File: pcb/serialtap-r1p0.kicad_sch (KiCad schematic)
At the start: 0 parts

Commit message: Capture the schematic, and correct the connector pin numbering
Two things that turned out to be one commit, because splitting them would
have left a snapshot where the schematic and the bench notes disagree about
which pin is which.

**The schematic is drawn.** `pcb/serialtap-r1p0.kicad_sch`, KiCad 10 native,
one A3 sheet in seven blocks, 43 components and 57 nets, transcribed from the
wiring contract in docs/schematic-capture.md. `kicad-cli sch erc
--severity-all` reports 0 violations, and every review invariant was checked
against the extracted netlist rather than the drawing — a drawing can look
right and still be wrong.

Decided at capture, with reasoning in docs/schematic-capture.md:

- `RILIM` = 66.5 kohm 1%, a 351-449 mA limit once part and resistor tolerance
  are counted: above the board's 250 mA worst case so a Wi-Fi burst cannot
  nuisance-trip it, below the rail's OEM-implied capability (ADR 0007)
- FAULT, PG and ST go to test pads, not GPIOs. Zero BOM cost, no firmware
  coupling; the cost is that no fault state reaches Home Assistant
- LM66200 VOUT_2 becomes a passive pin. Pins 2 and 7 are one internal node,
  and two power outputs on a net is an ERC conflict. The departure from the
  datasheet I/O column is recorded in lib/README.md
- Eleven generic symbols (R, C, LED, SW_Push, TestPoint, PWR_FLAG and the
  rails) copied in from KiCad 10, so the design still references nothing
  outside this repo. Passives carry no footprint: the package follows the MPN,
  and those are not pinned yet

kicad-happy review gate 1 ran. Of four non-informational findings, three
triage out and one is real and now accepted rather than fixed: USB VBUS has no
TVS, and reaches the LM66200's 6 V absolute maximum unclamped. The USB port is
a one-off setup interface and the operational path is J1, so the exposure is
closer to a debug header's.

**The service connector was being read from the wrong end.** Corrected order
is 5 V, TX, RX, spare, GND; old pin n is new pin 6 - n. Noth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
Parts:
- added C1, C7, C8, C9: 0.1u, symbol serialtap:C
- added C10, C5: 10u, symbol serialtap:C
- added C11, C2, C3: 1u, symbol serialtap:C
- added C4: 470u, symbol serialtap:C
- added C6: 22u, symbol serialtap:C
- added D1: LED, symbol serialtap:LED
- added J1: B05B-XASK-1-A, serialtap:JST_XA_B05B-XASK-1-A_1x05_P2.50mm_Vertical, symbol serialtap:B05B-XASK-1-A
- added J2: USB4085-GF-A, serialtap:USB_C_Receptacle_GCT_USB4085, symbol serialtap:USB4085-GF-A
- added L1: XGL4020-222MEC, serialtap:L_Coilcraft_XGL4020_4.0x4.0mm, symbol serialtap:XGL4020-222MEC
- added R1, R2: 330, symbol serialtap:R
- added R10, R9: 10k, symbol serialtap:R
- added R3, R4, R8: 5.1k, symbol serialtap:R
- added R5: 66.5k, symbol serialtap:R
- added R6, R7: 100k, symbol serialtap:R
- added SW1, SW2: SW_Push, symbol serialtap:SW_Push
- added TP1, TP10, TP2, TP3, TP4, TP5, TP6, TP7, TP8, TP9: TestPoint, symbol serialtap:TestPoint
- added U1: TPS2553DBV, serialtap:SOT-23-6, symbol serialtap:TPS2553DBV
- added U2: LM66200DRL, serialtap:TI_DRL0008A_SOT-5X3-8_2.1x1.6mm_P0.5mm, symbol serialtap:LM66200DRL
- added U3: TPS62162DSG, serialtap:Texas_DSG0008A_WSON-8-1EP_2x2mm_P0.5mm_EP0.9x1.6mm_ThermalVias, symbol serialtap:TPS62162DSG
- added U4: TXU0204RUT, serialtap:TI_RUT0012A_UQFN-12_2.0x1.7mm_P0.4mm, symbol serialtap:TXU0204RUT
- added U5: TPD4E05U06DQA, serialtap:USON-10_2.5x1.0mm_P0.5mm, symbol serialtap:TPD4E05U06DQA
- added U6: ESP32-C3-MINI-1, serialtap:ESP32-C3-MINI-1, symbol serialtap:ESP32-C3-MINI-1
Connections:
- new net: J2.A5 (CC1), R3.1
- new net: J2.B5 (CC2), R4.1
- new net: L1.1, U3.7 (SW)
- new net: R5.1, U1.5 (ILIM)
- new net: D1.2 (A), R8.2
- new net BOOT: R9.2, SW1.2, U6.23 (GPIO9)
- new net C3_EN: C11.1, R10.2, SW2.2, U6.8 (EN/CHIP_PU)
- new net C3_RX: TP7.1, U4.4 (A3Y), U6.19 (GPIO5/ADC2_CH0)
- new net C3_TX: TP6.1, U4.2 (A1), U6.18 (GPIO4/ADC1_CH4)
- new net EFUSE_OUT: C2.1, U1.6 (OUT), U2.3 (VIN1)
- new net FAULT_N: R6.2, TP8.1, U1.4 (~{FAULT})
- new net GND: C1.2, C10.2, C11.2, C2.2, C3.2, C4.2, C5.2, C6.2, C7.2, C8.2, C9.2, D1.1 (K), J1.5 (Pin_5), J2.A1 (GND), J2.A12 (GND), J2.B1 (GND), J2.B12 (GND), J2.SH (SHIELD), R3.2, R4.2, R5.2, SW1.1, SW2.1, TP3.1, U1.2 (GND), U2.1 (GND_1), U2.4 (~{ON}), U2.5 (GND_2), U3.1 (PGND), U3.4 (AGND), U3.5 (FB), U3.9 (PAD), U4.3 (A2), U4.6 (GND), U4.7 (B4), U5.3 (GND), U5.8 (GND), U6.1 (GND), U6.11 (GND), U6.14 (GND), U6.2 (GND), U6.36 (GND), U6.37 (GND), U6.38 (GND), U6.39 (GND), U6.40 (GND), U6.41 (GND), U6.42 (GND), U6.43 (GND), U6.44 (GND), U6.45 (GND), U6.46 (GND), U6.47 (GND), U6.48 (GND), U6.49 (GND), U6.50 (GND), U6.51 (GND), U6.52 (GND), U6.53 (GND)
- new net PG: R7.2, TP9.1, U3.8 (PG)
- new net PORT_5V: C1.1, J1.1 (Pin_1), U1.1 (IN), U1.3 (EN)
- new net PORT_RX: J1.3 (Pin_3), R2.1, U5.2 (D1-)
- new net PORT_TX: J1.2 (Pin_2), R1.1, U5.1 (D1+)
- new net RX_BUF: R2.2, TP5.1, U4.8 (B3)
- new net ST: TP10.1, U2.8 (ST)
- new net TX_BUF: R1.2, TP4.1, U4.10 (B1Y)
- new net USB_DM: J2.A7 (D-), J2.B7 (D-), U5.5 (D2-), U6.26 (GPIO18/USB_D-)
- new net USB_DP: J2.A6 (D+), J2.B6 (D+), U5.4 (D2+), U6.27 (GPIO19/USB_D+)
- new net USB_VBUS: C3.1, J2.A4 (VBUS), J2.A9 (VBUS), J2.B4 (VBUS), J2.B9 (VBUS), U2.6 (VIN2)
- new net V3V3: C10.1, C6.1, C7.1, C9.1, L1.2, R10.1, R7.1, R9.1, TP2.1, U3.6 (VOS), U4.1 (VCCA), U4.12 (OE), U6.3 (3V3)
- new net V5: C4.1, C5.1, C8.1, R6.1, R8.1, TP1.1, U2.2 (VOUT_1), U2.7 (VOUT_2), U3.2 (VIN), U3.3 (EN), U4.11 (VCCB)
- no-connect marks 0 -> 19
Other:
- note added: "A Service port - J1, ESD, UART series protection"
- note added: "B USB-C - programming, logging, bench power"
- note added: "Both sides of each translator channel, both rails, GND,"
- note added: "C Power path - eFuse, ideal-diode OR, 3.3 V buck"
- note added: "Channels 1 and 2 run A to B, 3 and 4 run B to A."
- note added: "D Level translation - fixed direction, 3.3 V <-> 5 V"
- note added: "Direction is fixed in silicon - ADR 0001."
- note added: "E ESP32-C3-MINI-1 - USB, UART, recovery"
- note added: "ESD channels tap each line on the connector side,"
- note added: "F Test access - SPDD 5.7"
- note added: "G ERC power sources"
- note added: "GPIO4 = UART1 TX, GPIO5 = UART1 RX, to the A side of U4."
- note added: "J1 pin 4: function unknown, deliberately unconnected"
- note added: "R5 sets the limit above the board's 250 mA worst case and"
- note added: "Shield to GND; no VBUS path to PORT_5V except through U2"
- note added: "Spare GPIOs carry explicit no-connects - ADR 0002."
- note added: "U1 EN is tied to IN: the appliance branch is always enabled."
- note added: "U3 FB goes to AGND and VOS senses at C6, per the datasheet;"
- note added: "V5 is driven by U2's output pin. The other three supplies enter"
- note added: "VOS is in the control loop - see docs/layout-rules.md."
- note added: "ahead of R1/R2 and of the USB pair"
- note added: "and the three diagnostic pins."
- note added: "below the rail's OEM-implied capability - ADR 0007."
- note added: "on passive connector pins, so each needs a flag for ERC."

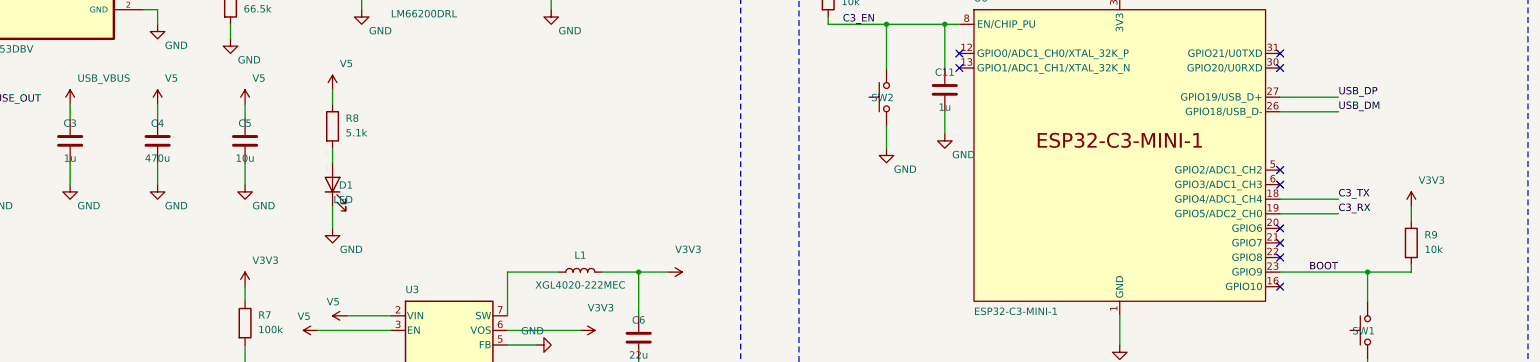
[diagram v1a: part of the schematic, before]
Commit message: Pin every passive, and let the switch datasheet move a resistor
Closes the last part-detail gate: all 22 BOM lines now carry an MPN, a
footprint and a datasheet. ~US$13.82/board.

Chosen as two families rather than line by line, because consistency is
worth more here than per-line optimisation:

- One KOA RK73H 1J series for every resistor value: 1%, 100 ppm/degC,
  -55..+155 C. The 66.5 kohm RILIM has to be 1% because the TPS2553
  datasheet says so, and running that grade everywhere costs cents and
  removes a class of mistake. Size code 1J = 0603 and tolerance code F =
  1% confirmed from the ordering table
- One Samsung CL series for every ceramic, X7R only and >=25 V. The
  TPS62162's LC stability table assumes variation stays inside +-20%
  *including DC bias*, which rules out X5R and 16 V parts on a 5 V rail.
  Samsung publish no per-part bias curve, so the retention estimate is
  labelled inference, not vendor data
- LTST-C191KGKT for the power LED: -55..+85 C, chosen over a 5x brighter
  emerald-green sibling for temperature grade, consistent with the
  H-grade module and the -Q1 ESD array. Dim is intended (SPDD 5.7)

**The switch datasheet changed a resistor.** C&K specify a 1 mA minimum
contact current; with a 10 kohm pull-up SW1 would have switched 0.33 mA,
a third of that, in the dry-circuit region where contact films do not
break down. R9 is therefore 2.2 kohm, putting 1.5 mA through SW1. R10
stays 10 kohm: SW2 discharges C11 through its contacts on every press,
which is a far larger wetting pulse, and shortening the EN time constant
would be the wrong move while the manual-reset anomaly is unexplained.

KMR211NGLFS's `NG` is the ordering key's no-ground-pin option, which is
what picks the four-pad land pattern over the five-pad one. C&K's
recommended layout - 0.9 x 1.0 mm pads at +-2.05, +-0.8 mm - matches
KiCad's footprint exactly. The datasheet had to be fetched by hand;
C&K and Littelfuse both refuse automated access.

Two capture defects, found by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
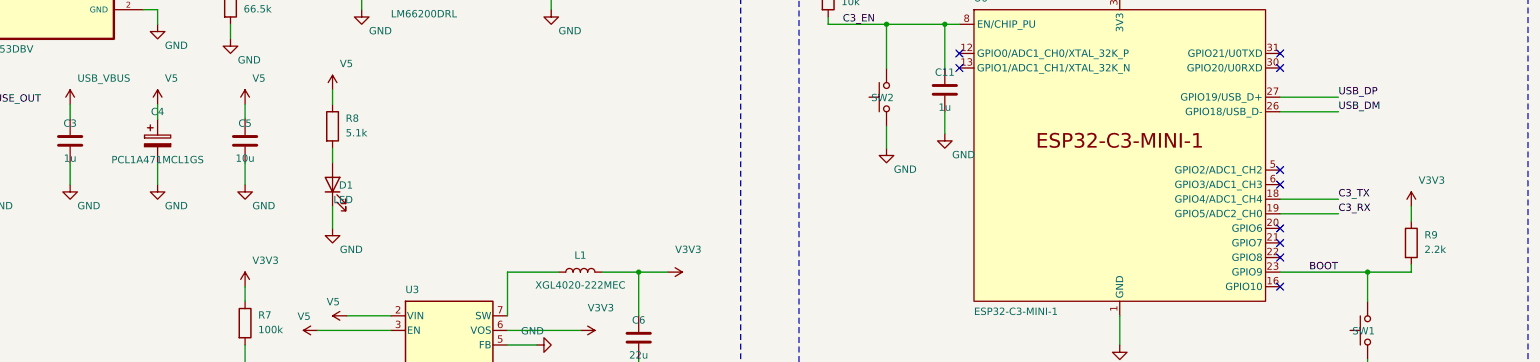
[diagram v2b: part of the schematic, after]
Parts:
- C1, C7, C8, C9: footprint (none) -> serialtap:C_0603_1608Metric; MPN (none) -> CL10B104KB8NNNC; Manufacturer (none) -> Samsung Electro-Mechanics
- C10, C5: footprint (none) -> serialtap:C_1206_3216Metric; MPN (none) -> CL31B106KAHNNNE; Manufacturer (none) -> Samsung Electro-Mechanics
- C11, C2, C3: footprint (none) -> serialtap:C_0603_1608Metric; MPN (none) -> CL10B105KA8NNNC; Manufacturer (none) -> Samsung Electro-Mechanics
- C4: value 470u -> PCL1A471MCL1GS; footprint (none) -> serialtap:CP_Elec_8x10; symbol serialtap:C -> serialtap:PCL1A471MCL1GS; MPN (none) -> PCL1A471MCL1GS; Manufacturer (none) -> Nichicon
- C6: footprint (none) -> serialtap:C_1210_3225Metric; MPN (none) -> CL32B226KAJNNNE; Manufacturer (none) -> Samsung Electro-Mechanics
- D1: footprint (none) -> serialtap:LED_0603_1608Metric; MPN (none) -> LTST-C191KGKT; Manufacturer (none) -> Lite-On
- R1, R2: footprint (none) -> serialtap:R_0603_1608Metric; MPN (none) -> RK73H1JTTD3300F; Manufacturer (none) -> KOA Speer
- R10: footprint (none) -> serialtap:R_0603_1608Metric; MPN (none) -> RK73H1JTTD1002F; Manufacturer (none) -> KOA Speer
- R3, R4, R8: footprint (none) -> serialtap:R_0603_1608Metric; MPN (none) -> RK73H1JTTD5101F; Manufacturer (none) -> KOA Speer
- R5: footprint (none) -> serialtap:R_0603_1608Metric; MPN (none) -> RK73H1JTTD6652F; Manufacturer (none) -> KOA Speer
- R6, R7: footprint (none) -> serialtap:R_0603_1608Metric; MPN (none) -> RK73H1JTTD1003F; Manufacturer (none) -> KOA Speer
- R9: value 10k -> 2.2k; footprint (none) -> serialtap:R_0603_1608Metric; MPN (none) -> RK73H1JTTD2201F; Manufacturer (none) -> KOA Speer
- SW1, SW2: footprint (none) -> serialtap:SW_Push_1P1T_NO_CK_KMR2; MPN (none) -> KMR211NGLFS; Manufacturer (none) -> C&K (Littelfuse)
- TP1, TP10, TP2, TP3, TP4, TP5, TP6, TP7, TP8, TP9: footprint (none) -> serialtap:TestPoint_Pad_D1.5mm; now left out of the parts list

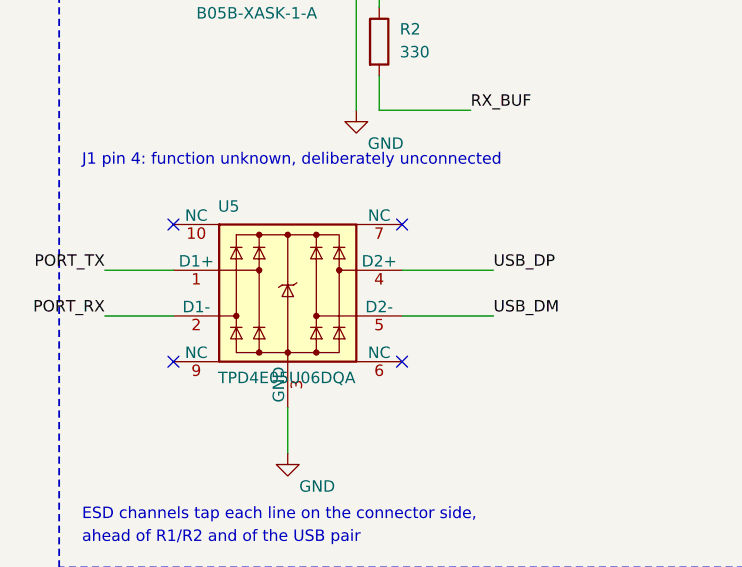
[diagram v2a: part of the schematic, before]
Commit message: Place and route r1p0, and fix three library defects on the way
Netlist imported into the PCB, all 43 footprints placed inside the
22 x 54 mm outline with the module's antenna keepout on-board (the slot
is the whole envelope, so no overhang), and all 138 connections routed:
signals and parts on L1, solid GND on L2, a V5 pour plus 3V3 traces on
L3, GND on L4 with the ten test points as bare pads. DRC is clean apart
from silkscreen warnings; zero unconnected, schematic parity zero.

The TVS channel assignment was swapped in the schematic so the USB pair
enters pins 1/2 and the UART pins 4/5 - the only order that routes the
pair to the array without a crossing. Net-class patterns (Power, USB)
now actually apply to nets; they were defined but unassigned.

Library defects found by the first DRC and render, fixed in lib/ and on
the board: the LM66200 footprint had no courtyard, the TPS62162 thermal
vias were drilled at 0.2 mm against the 0.25 mm fab minimum, and the JST
XA 3D model sat 10 mm off its pads.

Compromises still to record in the layout rules: the UART from the JST
runs on L3 with L1 hops (TVS 9 mm from the JST, 3 mm from the USB-C),
one TVS stub uses L3, CC2 passes under the USB-C body, and L4 carries
test-point pads. Fiducials, silkscreen tidy and review gate 2 remain.

Co-Authored-By: Claude Fable 5.1 <noreply@anthropic.com>
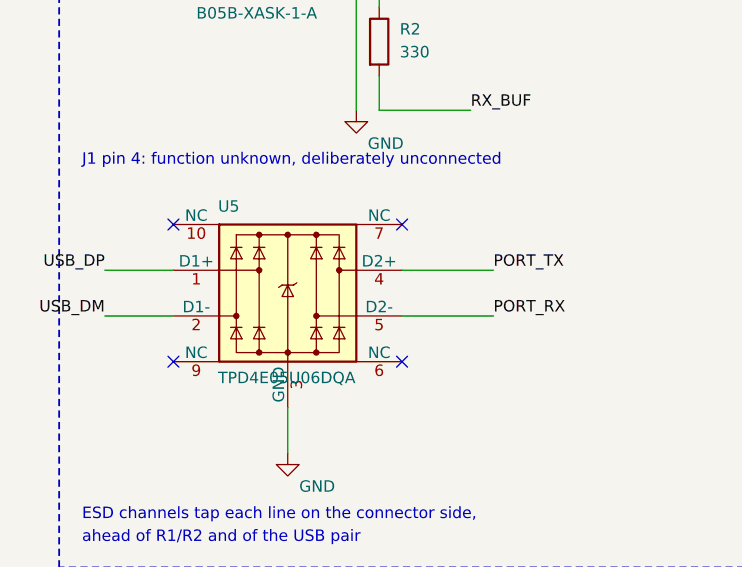
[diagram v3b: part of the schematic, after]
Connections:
- net PORT_RX: now also U5.5 (D2-); no longer U5.2 (D1-)
- net PORT_TX: now also U5.4 (D2+); no longer U5.1 (D1+)
- net USB_DM: now also U5.2 (D1-); no longer U5.5 (D2-)
- net USB_DP: now also U5.1 (D1+); no longer U5.4 (D2+)
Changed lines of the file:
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@@
 		)
 	)
-	(label "PORT_RX"
+	(label "USB_DM"
 		(at 20.32 76.2 180)
 		(effects
@@
 		)
 	)
-	(label "PORT_TX"
+	(label "USB_DP"
 		(at 20.32 71.12 180)
 		(effects
@@
 		)
 	)
-	(label "USB_DP"
+	(label "PORT_TX"
 		(at 63.5 71.12 0)
 		(effects
@@
 		)
 	)
-	(label "USB_DM"
+	(label "PORT_RX"
 		(at 63.5 76.2 0)
 		(effects
